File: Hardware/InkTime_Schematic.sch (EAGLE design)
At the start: 105 parts, among them IC1 RT6160AWSC, IC2 BMA423, IC3 BQ25180YBGR, IC4 DRV2605YZFR, J1 TC2030-IDC, J2 503480-2400, J4 KH-TYPE-C-16P_KH-TYPE-C-16P, Q1 20V/4.2A/52mΩ/1.4W, Q3 SI1308EDL-T1-GE3, U1 MAX17048G+T10, X1 32MHZ, X2 32.768KHZ

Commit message: Rerouted some signals
Signed-off-by: Andrei Rusanescu <andreirusanescu154@gmail.com>
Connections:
- removed net 3V3/1.7D: C34.1, IC4.VDD, Q1.S, R_PWR_EPD.2
- removed net 3V3/2.4A: C12.1, C14.1, C19.1, C7.1, C8.1, IC2.CSB, IC2.VDD, IC2.VDDIO, J1.1, NRF52840_QF.VDD@A22, NRF52840_QF.VDD@AD14, NRF52840_QF.VDD@AD23, NRF52840_QF.VDD@B1, TP_3.3V.TP, TP_3V3.TP
- removed net ALERT/1.6C: U1.!ALERT
- removed net ALERT/2.5C: NRF52840_QF.P0.10/NFC2@J24
- removed net D+/1.5D: D3.I/O2_2
- removed net D+/2.7D: NRF52840_QF.D+@AD6
- removed net D-/1.5D: D3.I/O1_2
- removed net D-/2.7D: NRF52840_QF.D-@AD4
- removed net EPD_BUSY/1.5D: J2.9
- removed net EPD_BUSY/2.2D: NRF52840_QF.P0.17@AD12
- removed net EPD_CS/1.4C: J2.12
- removed net EPD_CS/2.2D: NRF52840_QF.P0.05/AIN3@K2
- removed net EPD_DC/1.5D: J2.11
- removed net EPD_DC/2.2D: NRF52840_QF.P0.15@AD10
- removed net EPD_RST/1.5D: J2.10
- removed net EPD_RST/2.2D: NRF52840_QF.P0.16@AC11
- removed net HAPTIC_EN/1.4C: IC4.EN
- removed net HAPTIC_EN/2.6A: NRF52840_QF.P0.11@T2
- removed net MOSI/1.5B: J2.14
- removed net MOSI/2.2D: NRF52840_QF.P0.03/AIN1@B13
- removed net P0.13/1.5D: C30.1, R7.1, SW_UP.2
- removed net P0.13/2.6C: NRF52840_QF.P0.13@AD8
- removed net P0.14/1.5D: C31.1, R8.1, SW_ENT.2
- removed net P0.14/2.7C: NRF52840_QF.P0.14@AC9
- removed net P1.01/1.6C: Q1.G, R_PWR_EPD.1
- removed net P1.01/2.4B: NRF52840_QF.P1.01@Y23
- removed net P1.02/1.6C: C29.1, R9.1, SW_DN.2
- removed net P1.02/2.8C: NRF52840_QF.P1.02@W24
- removed net SCK/1.5B: J2.13
- removed net SCK/2.2D: NRF52840_QF.P0.02/AIN0@A12
- removed net SCL/1.4C: IC4.SCL, U1.SCL
- removed net SCL/2.4C: IC2.SCX, IC3.SCL, NRF52840_QF.P0.07@M2, R1.1, R3.2, TP3.TP
- removed net SDA/1.4C: IC4.SDA, U1.SDA
- removed net SDA/2.4C: IC2.SDX, IC3.SDA, NRF52840_QF.P0.06@L1, R2.1, R4.2, TP4.TP
- removed net VBAT/1.2A: C27.1, U1.CELL, U1.VDD
- removed net VBAT/2.5C: C37.1, IC3.BAT
- removed net VBUS/1.5D: C42.1, C43.1, D3.VBUS, J4.VBUS
- removed net VBUS/2.6D: C21.1, C38.1, IC3.IN, NRF52840_QF.VBUS@AD2
- new net 3V3: C12.1, C14.1, C19.1, C34.1, C7.1, C8.1, IC2.CSB, IC2.VDD, IC2.VDDIO, IC4.VDD, J1.1, NRF52840_QF.VDD@A22, NRF52840_QF.VDD@AD14, NRF52840_QF.VDD@AD23, NRF52840_QF.VDD@B1, Q1.S, R_PWR_EPD.2, TP_3.3V.TP, TP_3V3.TP
- new net ALERT: NRF52840_QF.P0.10/NFC2@J24, U1.!ALERT
- new net D+: D3.I/O2_2, NRF52840_QF.D+@AD6
- new net D-: D3.I/O1_2, NRF52840_QF.D-@AD4
- new net EPD_BUSY: J2.9, NRF52840_QF.P0.17@AD12
- new net EPD_CS: J2.12, NRF52840_QF.P0.05/AIN3@K2
- new net EPD_DC: J2.11, NRF52840_QF.P0.15@AD10
- new net EPD_RST: J2.10, NRF52840_QF.P0.22@AD18
- new net HAPTIC_EN: IC4.EN, NRF52840_QF.P0.12@U1
- new net MOSI: J2.14, NRF52840_QF.P0.03/AIN1@B13
- new net P0.13: C30.1, NRF52840_QF.P0.13@AD8, R7.1, SW_UP.2
- new net P0.14: C31.1, NRF52840_QF.P0.20@AD16, R8.1, SW_ENT.2
- new net P1.01: NRF52840_QF.P1.01@Y23, Q1.G, R_PWR_EPD.1
- new net P1.02: C29.1, NRF52840_QF.P1.02@W24, R9.1, SW_DN.2
- new net SCK: J2.13, NRF52840_QF.P0.02/AIN0@A12
- new net SCL: IC2.SCX, IC3.SCL, IC4.SCL, NRF52840_QF.P0.07@M2, R1.1, R3.2, TP3.TP, U1.SCL
- new net SDA: IC2.SDX, IC3.SDA, IC4.SDA, NRF52840_QF.P0.06@L1, R2.1, R4.2, TP4.TP, U1.SDA
- new net VBAT: C27.1, C37.1, IC3.BAT, U1.CELL, U1.VDD
- new net VBUS: C21.1, C38.1, C42.1, C43.1, D3.VBUS, IC3.IN, J4.VBUS, NRF52840_QF.VBUS@AD2
- net IMU_INT2: now also NRF52840_QF.P1.08@P2; no longer NRF52840_QF.P1.09@R1
- net P0.20: now also NRF52840_QF.P0.14@AC9; no longer NRF52840_QF.P0.20@AD16
- net P0.22: now also NRF52840_QF.P0.16@AC11; no longer NRF52840_QF.P0.22@AD18
- net P0.24: now also NRF52840_QF.P0.24@AD20; no longer NRF52840_QF.P0.18/RESET@AC13
- net P1.09: now also NRF52840_QF.P1.09@R1; no longer NRF52840_QF.P1.08@P2
- net PMIC_INT: now also NRF52840_QF.P0.11@T2; no longer NRF52840_QF.P0.12@U1
- net RESET: now also NRF52840_QF.P0.18/RESET@AC13; no longer NRF52840_QF.P0.24@AD20

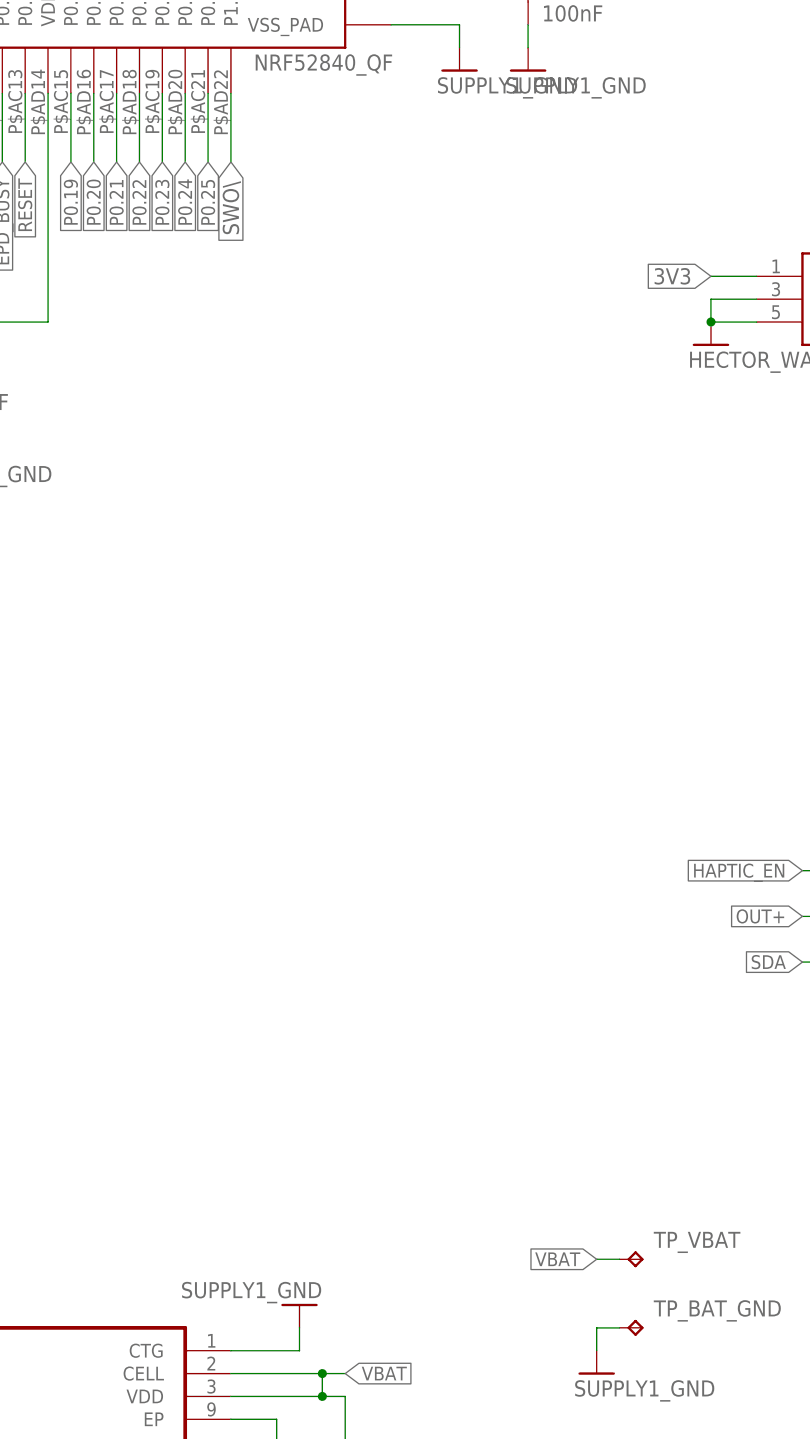
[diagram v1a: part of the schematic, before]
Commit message: Rerouted some more. Added BGA
Signed-off-by: Andrei Rusanescu <andreirusanescu154@gmail.com>
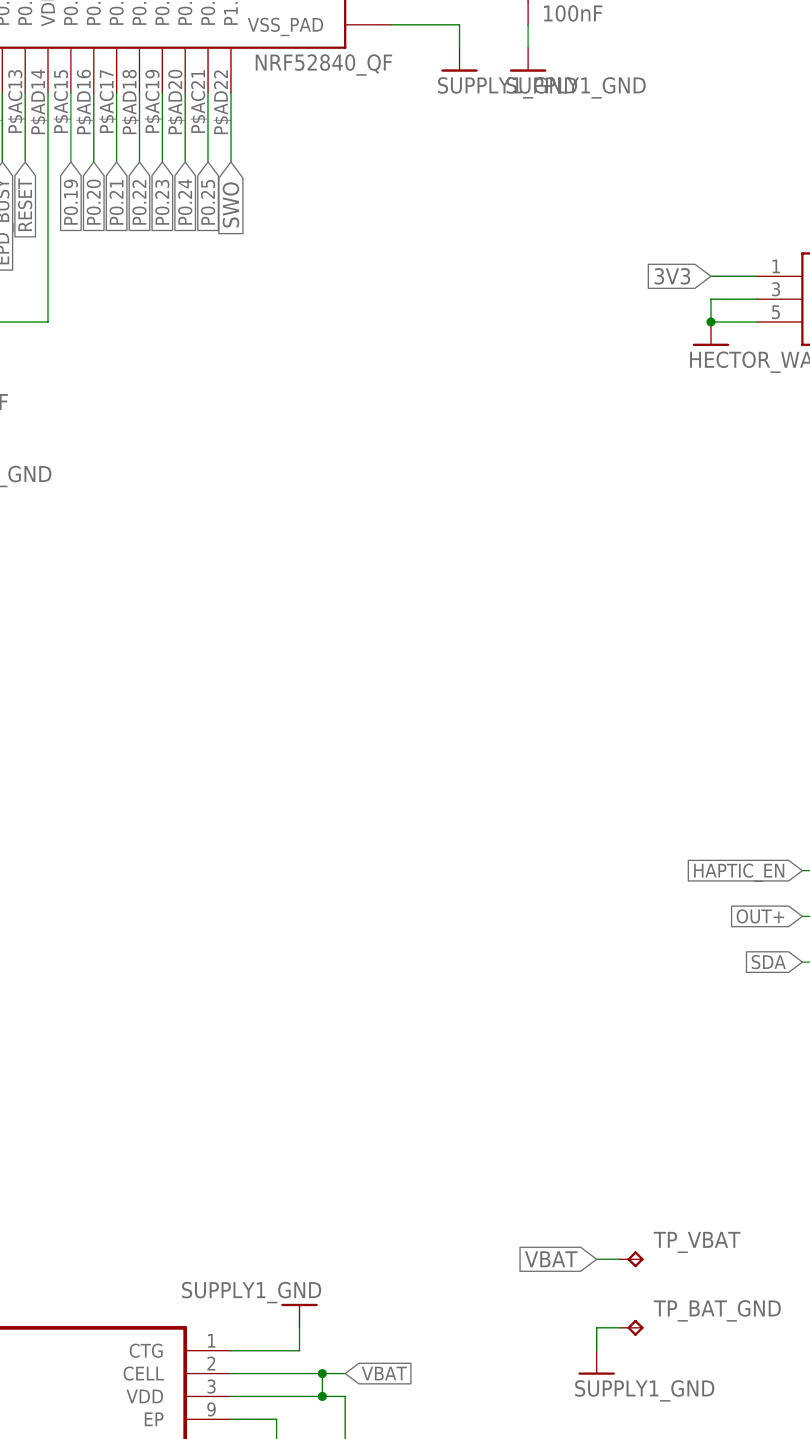
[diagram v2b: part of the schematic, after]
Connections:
- removed net N$33: TP_VBAT.TP
- removed net SWO\: NRF52840_QF.P1.00@AD22
- net EPD_RST: now also NRF52840_QF.P0.16@AC11; no longer NRF52840_QF.P0.22@AD18
- net P0.14: now also NRF52840_QF.P0.14@AC9; no longer NRF52840_QF.P0.20@AD16
- net P0.20: now also NRF52840_QF.P0.20@AD16; no longer NRF52840_QF.P0.14@AC9
- net P0.22: now also NRF52840_QF.P0.22@AD18; no longer NRF52840_QF.P0.16@AC11
- net SWO: now also NRF52840_QF.P1.00@AD22
- net VBAT: now also TP_VBAT.TP
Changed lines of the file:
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@@
 <class number="2" name="data_width" width="0" drill="0">
+</class>
+<class number="3" name="d_plus_minus" width="0" drill="0">
 </class>
 </classes>
@@
 </segment>
 </net>
-<net name="D-" class="2">
+<net name="D-" class="3">
 <segment>
 <pinref part="NRF52840_QF" gate="G$1" pin="D-@AD4"/>
@@
 </segment>
 </net>
-<net name="D+" class="2">
+<net name="D+" class="3">
 <segment>
 <pinref part="NRF52840_QF" gate="G$1" pin="D+@AD6"/>
@@
 </segment>
 <segment>
-<pinref part="NRF52840_QF" gate="G$1" pin="P0.20@AD16"/>
-<wire x1="60.96" y1="15.24" x2="60.96" y2="7.62" width="0.1524" layer="91"/>
+<pinref part="NRF52840_QF" gate="G$1" pin="P0.14@AC9"/>
+<wire x1="43.18" y1="15.24" x2="43.18" y2="10.16" width="0.1524" layer="91"/>
 <label x="43.18" y="10.16" size="1.524" layer="95" rot="R270" xref="yes"/>
 </segment>
@@
 </segment>
 <segment>
-<pinref part="NRF52840_QF" gate="G$1" pin="P0.22@AD18"/>
-<wire x1="66.04" y1="15.24" x2="66.04" y2="7.62" width="0.1524" layer="91"/>
+<pinref part="NRF52840_QF" gate="G$1" pin="P0.16@AC11"/>
+<wire x1="48.26" y1="15.24" x2="48.26" y2="7.62" width="0.1524" layer="91"/>
 <label x="48.26" y="7.62" size="1.524" layer="95" rot="R270" xref="yes"/>
 </segment>
@@
 <wire x1="73.66" y1="15.24" x2="73.66" y2="7.62" width="0.1524" layer="91"/>
 <label x="73.66" y="7.62" size="1.524" layer="95" rot="R270" xref="yes"/>
-</segment>
-</net>
-<net name="SWO\" class="2">
-<segment>
-<pinref part="NRF52840_QF" gate="G$1" pin="P1.00@AD22"/>
-<wire x1="76.2" y1="15.24" x2="76.2" y2="7.62" width="0.1524" layer="91"/>
-<label x="76.2" y="7.62" size="1.778" layer="95" rot="R270" xref="yes"/>
 </segment>
 </net>
@@
 <label x="-33.02" y="22.86" size="1.778" layer="95" rot="R180" xref="yes"/>
 </segment>
+<segment>
+<pinref part="NRF52840_QF" gate="G$1" pin="P1.00@AD22"/>
+<wire x1="76.2" y1="15.24" x2="76.2" y2="7.62" width="0.1524" layer="91"/>
+<label x="76.2" y="7.62" size="1.778" layer="95" rot="R270" xref="yes"/>
+</segment>
 </net>
 <net name="N$26" class="2">
@@
 <label x="-68.58" y="144.78" size="1.524" layer="95" xref="yes"/>
 <pinref part="C37" gate="C$1" pin="1"/>
-</segment>
-<segment>
-<label x="116.84" y="-114.3" size="1.524" layer="95" rot="R180" xref="yes"/>
 </segment>
 <segment>
@@
 <label x="88.9" y="-127" size="1.524" layer="95" xref="yes"/>
 <pinref part="C27" gate="C$1" pin="1"/>
+</segment>
+<segment>
+<pinref part="TP_VBAT" gate="G$1" pin="TP"/>
+<wire x1="119.38" y1="-114.3" x2="116.84" y2="-114.3" width="0.1524" layer="91"/>
+<label x="116.84" y="-114.3" size="1.778" layer="95" rot="R180" xref="yes"/>
 </segment>
 </net>
@@
 </segment>
 </net>
-<net name="N$33" class="2">
-<segment>
-<pinref part="TP_VBAT" gate="G$1" pin="TP"/>
-<wire x1="119.38" y1="-114.3" x2="116.84" y2="-114.3" width="0.1524" layer="91"/>
-</segment>
-</net>
 <net name="N$35" class="2">
 <segment>
@@
 </segment>
 </net>
-<net name="P0.20" class="2">
-<segment>
-<pinref part="NRF52840_QF" gate="G$1" pin="P0.14@AC9"/>
-<wire x1="43.18" y1="15.24" x2="43.18" y2="10.16" width="0.1524" layer="91"/>
-<label x="60.96" y="7.62" size="1.524" layer="95" rot="R270" xref="yes"/>
-</segment>
-</net>
-<net name="P0.22" class="2">
-<segment>
-<pinref part="NRF52840_QF" gate="G$1" pin="P0.16@AC11"/>
-<wire x1="48.26" y1="15.24" x2="48.26" y2="7.62" width="0.1524" layer="91"/>
-<label x="66.04" y="7.62" size="1.524" layer="95" rot="R270" xref="yes"/>
-</segment>
-</net>
 <net name="P0.26" class="2">
 <segment>
@@
 </segment>
 </net>
+<net name="P0.20" class="2">
+<segment>
+<pinref part="NRF52840_QF" gate="G$1" pin="P0.20@AD16"/>
+<wire x1="60.96" y1="15.24" x2="60.96" y2="7.62" width="0.1524" layer="91"/>
+<label x="60.96" y="7.62" size="1.524" layer="95" rot="R270" xref="yes"/>
+</segment>
+</net>
+<net name="P0.22" class="2">
+<segment>
+<pinref part="NRF52840_QF" gate="G$1" pin="P0.22@AD18"/>
+<wire x1="66.04" y1="15.24" x2="66.04" y2="7.62" width="0.1524" layer="91"/>
+<label x="66.04" y="7.62" size="1.524" layer="95" rot="R270" xref="yes"/>
+</segment>
+</net>
